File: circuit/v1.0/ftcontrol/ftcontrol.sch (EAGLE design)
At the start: 28 parts, among them IC1 7805, IC2 7805, IC3 ATMEGA328P-PU, IC4 L293D, J1 POWER_JACKPTH, J2 POWER_JACKPTH, J3 ISP, J4 SERVO, J5 PING, J6 MOTORS, Q1 16Mhz

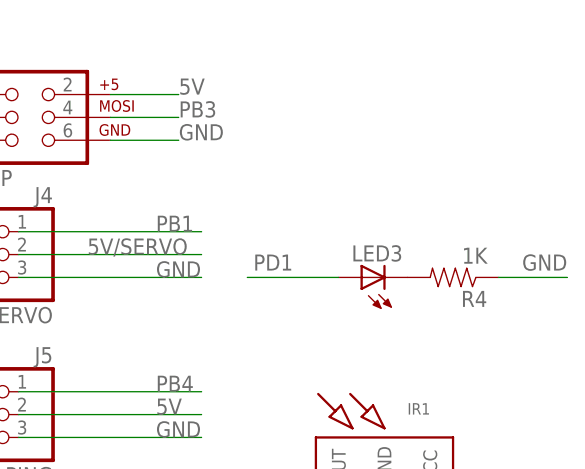
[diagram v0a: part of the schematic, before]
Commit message: moved servo/ping connectors
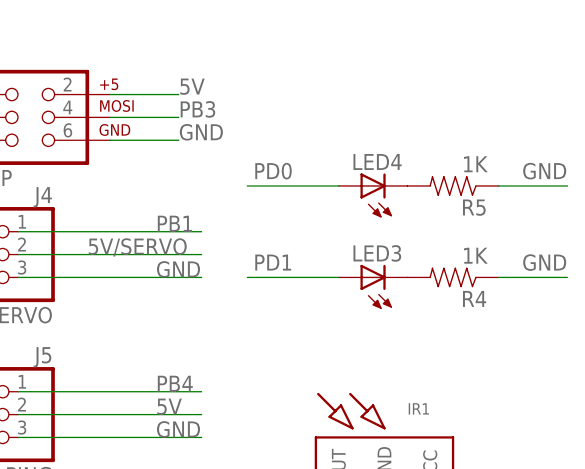
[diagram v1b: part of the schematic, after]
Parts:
- added LED4: (no value), adafruit:LED3MM
- added R5: 1K, SparkFun-Resistors:RESISTORPTH-1/4W
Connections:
- new net N$9: LED4.C, R5.2
- net GND: now also R5.1
- net PD0: now also LED4.A
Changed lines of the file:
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@@
 <part name="LED3" library="adafruit" deviceset="LED" device="3MM"/>
 <part name="IR1" library="ubiyubix" deviceset="IR_TSOP4838" device=""/>
+<part name="LED4" library="adafruit" deviceset="LED" device="3MM"/>
+<part name="R5" library="SparkFun-Resistors" deviceset="RESISTOR" device="PTH-1/4W" value="1K"/>
 </parts>
 <sheets>
@@
 <instance part="LED3" gate="G$1" x="106.68" y="88.9" rot="R90"/>
 <instance part="IR1" gate="G$1" x="109.22" y="66.04"/>
+<instance part="LED4" gate="G$1" x="106.68" y="99.06" rot="R90"/>
+<instance part="R5" gate="G$1" x="116.84" y="99.06" rot="R180"/>
 </instances>
 <busses>
@@
 <wire x1="109.22" y1="60.96" x2="109.22" y2="53.34" width="0.1524" layer="91"/>
 </segment>
+<segment>
+<pinref part="R5" gate="G$1" pin="1"/>
+<wire x1="121.92" y1="99.06" x2="129.54" y2="99.06" width="0.1524" layer="91"/>
+<label x="129.54" y="101.6" size="1.778" layer="95" rot="R180"/>
+</segment>
 </net>
 <net name="N$3" class="0">
@@
 <label x="33.02" y="33.02" size="1.778" layer="95"/>
 </segment>
+<segment>
+<pinref part="LED4" gate="G$1" pin="A"/>
+<wire x1="104.14" y1="99.06" x2="93.98" y2="99.06" width="0.1524" layer="91"/>
+<label x="99.06" y="101.6" size="1.778" layer="95" rot="R180"/>
+</segment>
 </net>
 <net name="PD1" class="0">
@@
 </segment>
 </net>
+<net name="N$9" class="0">
+<segment>
+<pinref part="LED4" gate="G$1" pin="C"/>
+<pinref part="R5" gate="G$1" pin="2"/>
+</segment>
+</net>

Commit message: imported firmware
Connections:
- removed net N$2: C1.+, D1.C, IC1.VI
- removed net PD2: IC3.(PCI18/INT0)PD2
- removed net PD5: IC3.(PCI21/T1/OC0B)PD5
- new net N$13: J1.PWR, S1.P
- net GND: now also J1.GND, J2.GND; no longer J1.PWR, J2.PWR
- net N$5: now also J2.PWR, S2.P; no longer D2.C, IC2.VI
- net VCC: now also C1.+, D1.C, IC1.VI; no longer J1.GND, S1.P
- net VCC/2: now also D2.C, IC2.VI; no longer J2.GND, S2.P
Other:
- moved on the sheet: J1, J2
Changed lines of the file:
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@@
 <part name="J5" library="adafruit" deviceset="PINHD-1X3" device="" value="PING"/>
 <part name="J6" library="pinhead" deviceset="PINHD-1X4" device="" value="MOTORS"/>
-<part name="P+1" library="supply1" deviceset="VCC" device=""/>
-<part name="P+2" library="supply1" deviceset="VCC/2" device=""/>
 <part name="LED1" library="adafruit" deviceset="LED" device="3MM"/>
 <part name="R2" library="SparkFun-Resistors" deviceset="RESISTOR" device="PTH-1/4W" value="1K"/>
@@
 <part name="LED4" library="adafruit" deviceset="LED" device="3MM"/>
 <part name="R5" library="SparkFun-Resistors" deviceset="RESISTOR" device="PTH-1/4W" value="1K"/>
+<part name="P+3" library="supply1" deviceset="VCC/2" device=""/>
+<part name="P+2" library="supply1" deviceset="VCC" device=""/>
 </parts>
 <sheets>
@@
 <attribute name="VALUE" x="-52.451" y="44.704" size="1.778" layer="96"/>
 </instance>
-<instance part="J1" gate="G$1" x="-40.64" y="114.3" rot="MR180"/>
+<instance part="J1" gate="G$1" x="-40.64" y="104.14"/>
 <instance part="S1" gate="1" x="-30.48" y="111.76"/>
 <instance part="C1" gate="G$1" x="-12.7" y="104.14" smashed="yes">
@@
 <instance part="IC1" gate="A1" x="2.54" y="109.22"/>
 <instance part="D1" gate="G$1" x="-20.32" y="109.22" smashed="yes">
-<attribute name="NAME" x="-17.78" y="107.1626" size="1.778" layer="95"/>
-<attribute name="VALUE" x="-17.78" y="110.7186" size="1.778" layer="96"/>
-</instance>
-<instance part="J2" gate="G$1" x="-40.64" y="88.9" rot="MR180"/>
+<attribute name="NAME" x="-25.4" y="104.1146" size="1.778" layer="95"/>
+<attribute name="VALUE" x="-25.4" y="101.5746" size="1.778" layer="96"/>
+</instance>
+<instance part="J2" gate="G$1" x="-40.64" y="78.74"/>
 <instance part="S2" gate="1" x="-30.48" y="86.36"/>
 <instance part="GND3" gate="1" x="2.54" y="71.12"/>
 <instance part="GND4" gate="1" x="-35.56" y="76.2"/>
 <instance part="IC2" gate="A1" x="2.54" y="83.82"/>
-<instance part="D2" gate="G$1" x="-20.32" y="83.82"/>
+<instance part="D2" gate="G$1" x="-20.32" y="83.82" smashed="yes">
+<attribute name="NAME" x="-22.86" y="78.7146" size="1.778" layer="95"/>
+<attribute name="VALUE" x="-17.526" y="78.7146" size="1.778" layer="96"/>
+</instance>
 <instance part="J3" gate="G$1" x="68.58" y="106.68"/>
 <instance part="GND7" gate="1" x="-50.8" y="22.86"/>
@@
 <instance part="J5" gate="A" x="66.04" y="73.66" rot="MR0"/>
 <instance part="J6" gate="A" x="66.04" y="53.34" rot="MR0"/>
-<instance part="P+1" gate="VCC" x="-38.1" y="114.3" smashed="yes">
-<attribute name="VALUE" x="-38.1" y="116.84" size="1.778" layer="96" rot="R180"/>
-</instance>
-<instance part="P+2" gate="G$1" x="-38.1" y="88.9" smashed="yes">
-<attribute name="VALUE" x="-38.1" y="93.98" size="1.778" layer="96" rot="R180"/>
-</instance>
 <instance part="LED1" gate="G$1" x="30.48" y="109.22" rot="R90"/>
 <instance part="R2" gate="G$1" x="38.1" y="104.14" rot="R270"/>
@@
 <instance part="LED4" gate="G$1" x="106.68" y="99.06" rot="R90"/>
 <instance part="R5" gate="G$1" x="116.84" y="99.06" rot="R180"/>
+<instance part="P+3" gate="G$1" x="-12.7" y="88.9" smashed="yes">
+<attribute name="VALUE" x="-12.7" y="93.98" size="1.778" layer="96" rot="R180"/>
+</instance>
+<instance part="P+2" gate="VCC" x="-12.7" y="114.3" smashed="yes">
+<attribute name="VALUE" x="-12.7" y="116.84" size="1.778" layer="96" rot="R180"/>
+</instance>
 </instances>
 <busses>
 </busses>
 <nets>
-<net name="N$2" class="0">
-<segment>
-<pinref part="C1" gate="G$1" pin="+"/>
-<wire x1="-12.7" y1="109.22" x2="-12.7" y2="106.68" width="0.1524" layer="91"/>
-<pinref part="IC1" gate="A1" pin="VI"/>
-<wire x1="-12.7" y1="109.22" x2="-7.62" y2="109.22" width="0.1524" layer="91"/>
-<pinref part="D1" gate="G$1" pin="C"/>
-<wire x1="-17.78" y1="109.22" x2="-12.7" y2="109.22" width="0.1524" layer="91"/>
-<junction x="-12.7" y="109.22"/>
-</segment>
-</net>
 <net name="5V" class="0">
 <segment>
@@
 </segment>
 <segment>
-<pinref part="J1" gate="G$1" pin="PWR"/>
-<pinref part="GND2" gate="1" pin="GND"/>
-<wire x1="-38.1" y1="106.68" x2="-35.56" y2="106.68" width="0.1524" layer="91"/>
-<wire x1="-35.56" y1="106.68" x2="-35.56" y2="104.14" width="0.1524" layer="91"/>
-</segment>
-<segment>
-<pinref part="J2" gate="G$1" pin="PWR"/>
-<pinref part="GND4" gate="1" pin="GND"/>
-<wire x1="-38.1" y1="81.28" x2="-35.56" y2="81.28" width="0.1524" layer="91"/>
-<wire x1="-35.56" y1="81.28" x2="-35.56" y2="78.74" width="0.1524" layer="91"/>
-</segment>
-<segment>
 <pinref part="IC3" gate="G$1" pin="AGND"/>
 <wire x1="-27.94" y1="53.34" x2="-33.02" y2="53.34" width="0.1524" layer="91"/>
@@
 <label x="129.54" y="101.6" size="1.778" layer="95" rot="R180"/>
 </segment>
+<segment>
+<pinref part="J2" gate="G$1" pin="GND"/>
+<wire x1="-38.1" y1="81.28" x2="-35.56" y2="81.28" width="0.1524" layer="91"/>
+<pinref part="GND4" gate="1" pin="GND"/>
+<wire x1="-35.56" y1="81.28" x2="-35.56" y2="78.74" width="0.1524" layer="91"/>
+</segment>
+<segment>
+<pinref part="J1" gate="G$1" pin="GND"/>
+<wire x1="-38.1" y1="106.68" x2="-35.56" y2="106.68" width="0.1524" layer="91"/>
+<pinref part="GND2" gate="1" pin="GND"/>
+<wire x1="-35.56" y1="106.68" x2="-35.56" y2="104.14" width="0.1524" layer="91"/>
+</segment>
 </net>
 <net name="N$3" class="0">
@@
 <pinref part="D1" gate="G$1" pin="A"/>
 <wire x1="-25.4" y1="109.22" x2="-22.86" y2="109.22" width="0.1524" layer="91"/>
-</segment>
-</net>
-<net name="N$5" class="0">
-<segment>
-<pinref part="IC2" gate="A1" pin="VI"/>
-<pinref part="D2" gate="G$1" pin="C"/>
-<wire x1="-17.78" y1="83.82" x2="-7.62" y2="83.82" width="0.1524" layer="91"/>
 </segment>
 </net>
@@
 </segment>
 </net>
-<net name="PD2" class="0">
-<segment>
-<pinref part="IC3" gate="G$1" pin="(PCI18/INT0)PD2"/>
-<wire x1="27.94" y1="27.94" x2="38.1" y2="27.94" width="0.1524" layer="91"/>
-<label x="33.02" y="27.94" size="1.778" layer="95"/>
-</segment>
-</net>
-<net name="PD5" class="0">
-<segment>
-<pinref part="IC3" gate="G$1" pin="(PCI21/T1/OC0B)PD5"/>
-<wire x1="27.94" y1="20.32" x2="38.1" y2="20.32" width="0.1524" layer="91"/>
-<label x="33.02" y="20.32" size="1.778" layer="95"/>
-</segment>
-</net>
 <net name="1Y" class="0">
 <segment>
@@
 </segment>
 <segment>
-<pinref part="J2" gate="G$1" pin="GND"/>
-<pinref part="S2" gate="1" pin="P"/>
-<wire x1="-38.1" y1="86.36" x2="-33.02" y2="86.36" width="0.1524" layer="91"/>
-<pinref part="P+2" gate="G$1" pin="VCC/2"/>
-<junction x="-38.1" y="86.36"/>
-</segment>
-</net>
-<net name="VCC" class="0">
-<segment>
-<pinref part="J1" gate="G$1" pin="GND"/>
-<pinref part="S1" gate="1" pin="P"/>
-<wire x1="-38.1" y1="111.76" x2="-33.02" y2="111.76" width="0.1524" layer="91"/>
-<pinref part="P+1" gate="VCC" pin="VCC"/>
-<junction x="-38.1" y="111.76"/>
+<pinref part="IC2" gate="A1" pin="VI"/>
+<pinref part="D2" gate="G$1" pin="C"/>
+<wire x1="-17.78" y1="83.82" x2="-12.7" y2="83.82" width="0.1524" layer="91"/>
+<pinref part="P+3" gate="G$1" pin="VCC/2"/>
+<wire x1="-12.7" y1="83.82" x2="-7.62" y2="83.82" width="0.1524" layer="91"/>
+<wire x1="-12.7" y1="86.36" x2="-12.7" y2="83.82" width="0.1524" layer="91"/>
+<junction x="-12.7" y="83.82"/>
 </segment>
 </net>
@@
 </segment>
 </net>
+<net name="N$5" class="0">
+<segment>
+<pinref part="J2" gate="G$1" pin="PWR"/>
+<pinref part="S2" gate="1" pin="P"/>
+<wire x1="-38.1" y1="86.36" x2="-33.02" y2="86.36" width="0.1524" layer="91"/>
+</segment>
+</net>
+<net name="N$13" class="0">
+<segment>
+<pinref part="J1" gate="G$1" pin="PWR"/>
+<pinref part="S1" gate="1" pin="P"/>
+<wire x1="-38.1" y1="111.76" x2="-33.02" y2="111.76" width="0.1524" layer="91"/>
+</segment>
+</net>
+<net name="VCC" class="0">
+<segment>
+<pinref part="C1" gate="G$1" pin="+"/>
+<wire x1="-12.7" y1="109.22" x2="-12.7" y2="106.68" width="0.1524" layer="91"/>
+<pinref part="IC1" gate="A1" pin="VI"/>
+<wire x1="-12.7" y1="109.22" x2="-7.62" y2="109.22" width="0.1524" layer="91"/>
+<pinref part="D1" gate="G$1" pin="C"/>
+<wire x1="-17.78" y1="109.22" x2="-12.7" y2="109.22" width="0.1524" layer="91"/>
+<junction x="-12.7" y="109.22"/>
+<pinref part="P+2" gate="VCC" pin="VCC"/>
+<wire x1="-12.7" y1="111.76" x2="-12.7" y2="109.22" width="0.1524" layer="91"/>
+</segment>
+</net>
